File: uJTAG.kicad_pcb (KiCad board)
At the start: 2 copper layers, 20 x 30 mm, 28 parts, among them J1 USB_3, P1 CONN_6, U1 FT232H, U2 LD3985M, X1 CRYSTAL

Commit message: updated header to conform to the AVR JTAG style.
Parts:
- P1: value CONN_6 -> AVR JTAG; footprint Pin_Headers:Pin_Header_Straight_2x05 -> Pin_Headers:Pin_Header_Angled_2x05
- moved P1 10.9 mm to (165.1, 124.6), turned to 270 degrees
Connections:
- P1 pad 1: /TMS -> /TCK
- P1 pad 10: (no net) -> GND
- P1 pad 2: /TDI -> GND
- P1 pad 4: /TCK -> Net-(D2-Pad2)
- P1 pad 5: GND -> /TMS
- P1 pad 6: Net-(D2-Pad2) -> (no net)
- P1 pad 9: (no net) -> /TDI
- U1 pad 26: (no net) -> 3V3
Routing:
- net /TCK: track 11.1 -> 17.8 mm
- net /TMS: track 11.3 -> 7.90 mm
- net /TDO: track 14.2 -> 11.5 mm, vias 1 -> 2
- net /TDI: track 8.14 -> 7.13 mm
- net GND: track 39.2 -> 38.3 mm, vias 7 -> 10
- net Net-(D2-Pad2): track 7.05 -> 6.37 mm

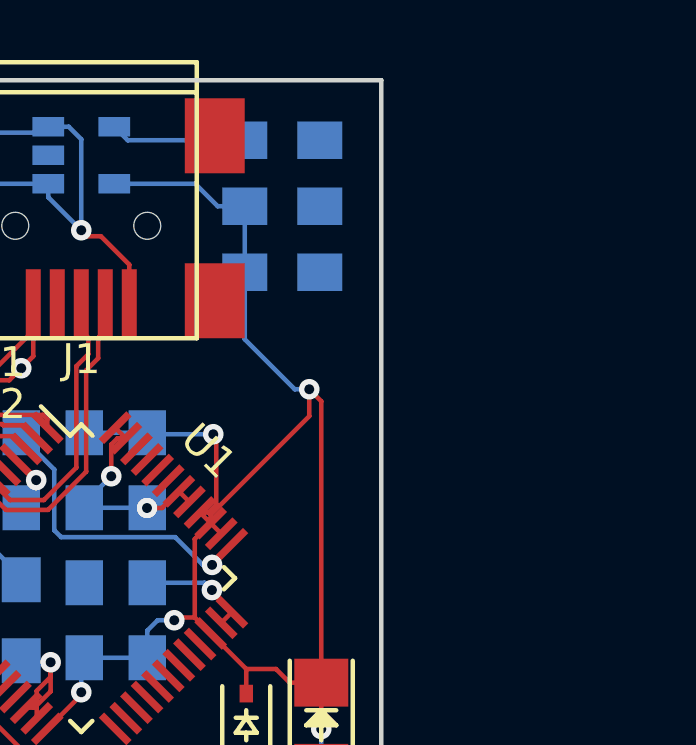
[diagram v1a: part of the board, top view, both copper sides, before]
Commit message: added silk screen url and version.
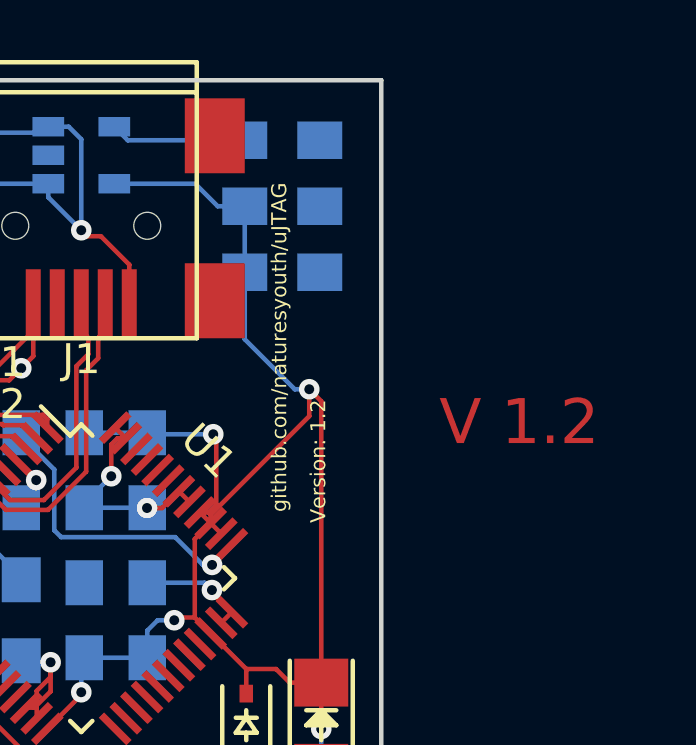
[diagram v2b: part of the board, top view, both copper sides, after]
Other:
- board text added: "V 1.2"
- board text added: "Version: 1.2"
- board text added: "github.com/naturesyouth/uJTAG"
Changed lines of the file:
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@@
     (area 149.924999 99.924999 170.075001 130.075001)
     (thickness 1.6)
-    (drawings 4)
+    (drawings 7)
     (tracks 276)
     (zones 0)
@@
   (page A4)
   (layers
-    (0 F.Cu signal)
-    (31 B.Cu signal)
-    (32 B.Adhes user)
-    (33 F.Adhes user)
-    (34 B.Paste user)
-    (35 F.Paste user)
-    (36 B.SilkS user)
+    (0 F.Cu signal hide)
+    (31 B.Cu signal hide)
+    (32 B.Adhes user hide)
+    (33 F.Adhes user hide)
+    (34 B.Paste user hide)
+    (35 F.Paste user hide)
+    (36 B.SilkS user hide)
     (37 F.SilkS user)
-    (38 B.Mask user)
-    (39 F.Mask user)
-    (40 Dwgs.User user)
-    (41 Cmts.User user)
-    (42 Eco1.User user)
-    (43 Eco2.User user)
-    (44 Edge.Cuts user)
-    (45 Margin user)
-    (46 B.CrtYd user)
-    (47 F.CrtYd user)
-    (48 B.Fab user)
-    (49 F.Fab user)
+    (38 B.Mask user hide)
+    (39 F.Mask user hide)
+    (40 Dwgs.User user hide)
+    (41 Cmts.User user hide)
+    (42 Eco1.User user hide)
+    (43 Eco2.User user hide)
+    (44 Edge.Cuts user hide)
+    (45 Margin user hide)
+    (46 B.CrtYd user hide)
+    (47 F.CrtYd user hide)
+    (48 B.Fab user hide)
+    (49 F.Fab user hide)
   )
   (setup
@@
     )
   )
+  (gr_text "Version: 1.2" (at 167.9 112.7 90) (layer F.SilkS)
+    (effects (font (size 0.5 0.5) (thickness 0.125)))
+  )
+  (gr_text "V 1.2" (at 174.6 111.4) (layer F.Cu)
+    (effects (font (size 1.5 1.5) (thickness 0.3)))
+  )
+  (gr_text github.com/naturesyouth/uJTAG (at 166.6 108.9 90) (layer F.SilkS)
+    (effects (font (size 0.5 0.5) (thickness 0.125)))
+  )
   (gr_line (start 150 130) (end 150 100) (layer Edge.Cuts) (width 0.15))
